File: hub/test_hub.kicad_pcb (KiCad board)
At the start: 2 copper layers, 88.9 x 76.2 mm, 108 parts, among them J1 ARM-SWD, P1 USB_OTG, P2 5V_SEL, P3 5V_EXT, P4 USB1, P5 USB2, P6 USB3, P7 UART, SW1 RST, SW2 BOOT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

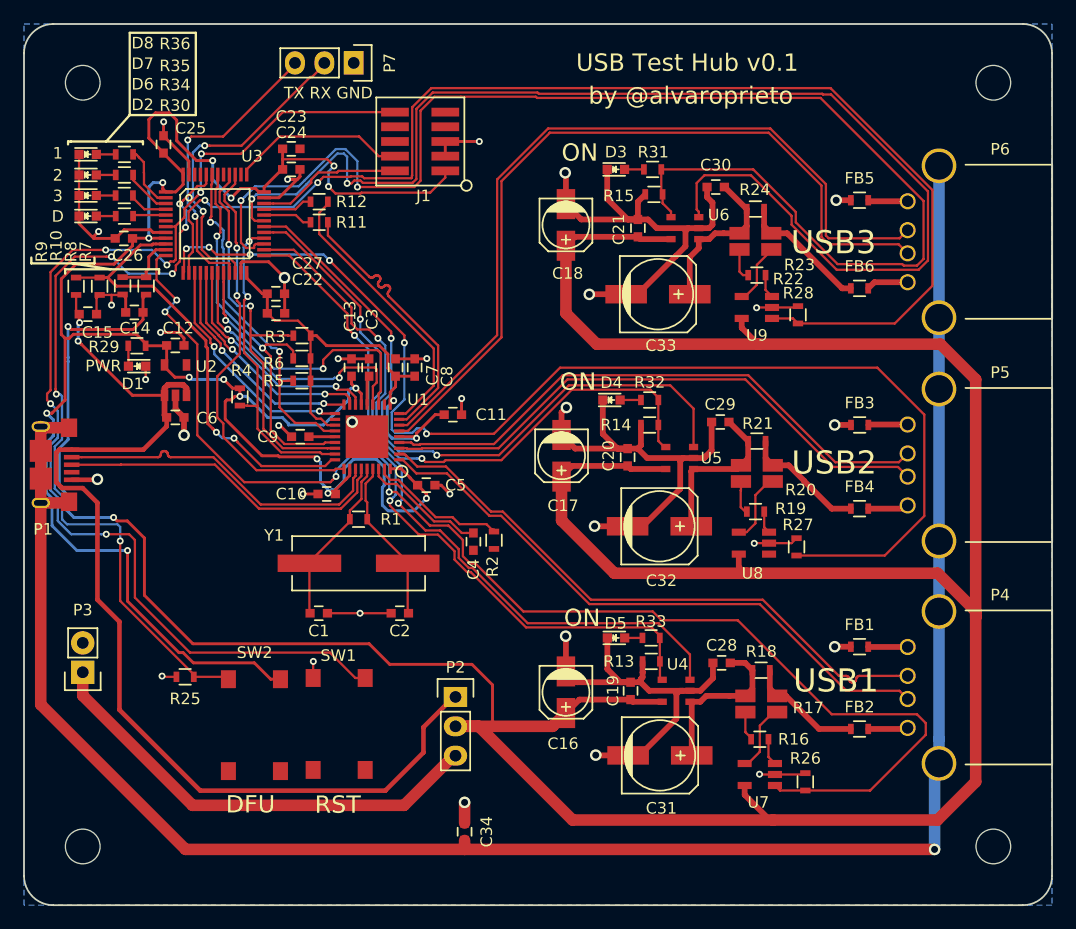
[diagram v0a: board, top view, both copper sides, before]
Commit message: Fixing unconnected pads....
Not sure how I missed so many unconnected things :(
MAKE SURE YOU CLICK ON "LIST UNCONNECTED" AFTER RUNNING DRC!!!!!!!!!!!
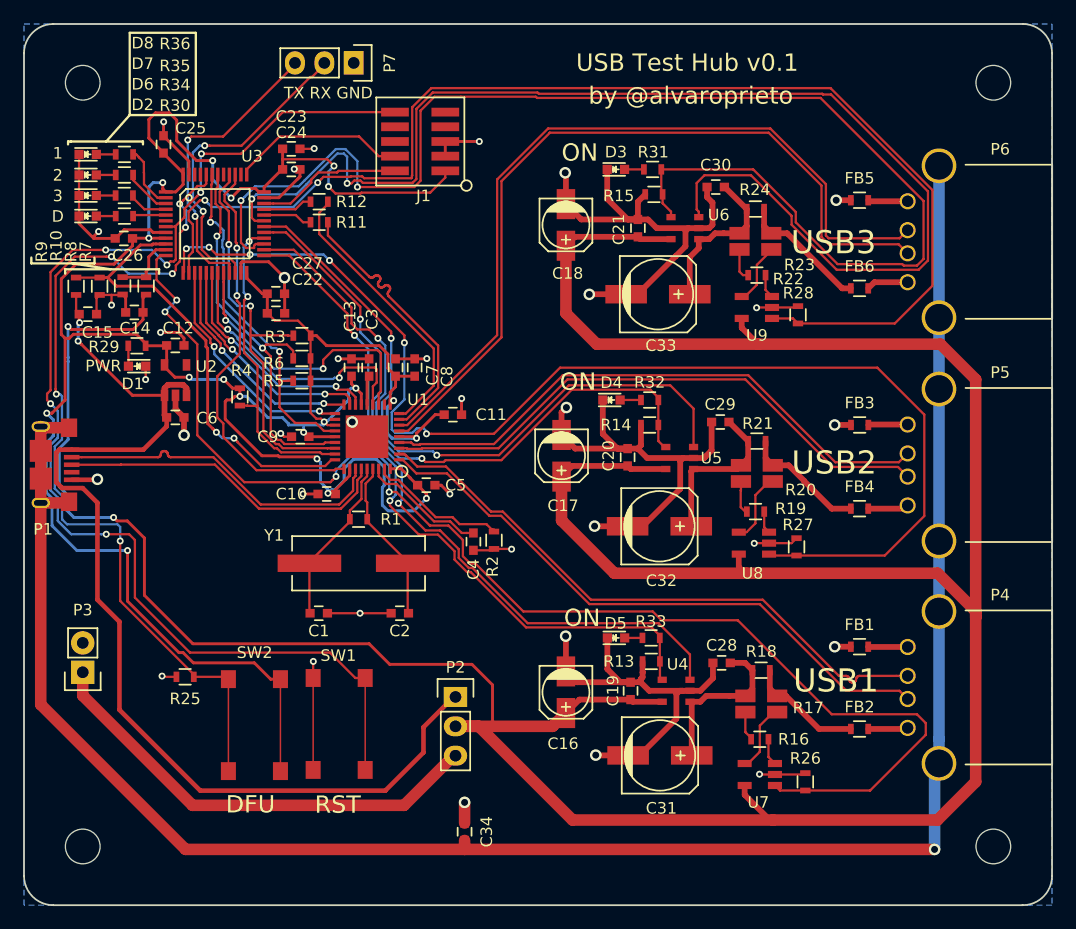
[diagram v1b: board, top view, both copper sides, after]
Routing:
- net GND: track 206.7 -> 218.5 mm, vias 33 -> 35
- net +3V3: track 234.6 -> 244.4 mm, vias 17 -> 19
- net /BOOT0: track 67.9 -> 75.9 mm
- net /nRST: track 99.2 -> 107.1 mm
- net /SNS2: track 104.8 -> 107.2 mm
